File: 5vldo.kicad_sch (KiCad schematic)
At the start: 11 parts, among them IC1 TPS7A4501KTTR, IC2 TPS7A4501KTTR

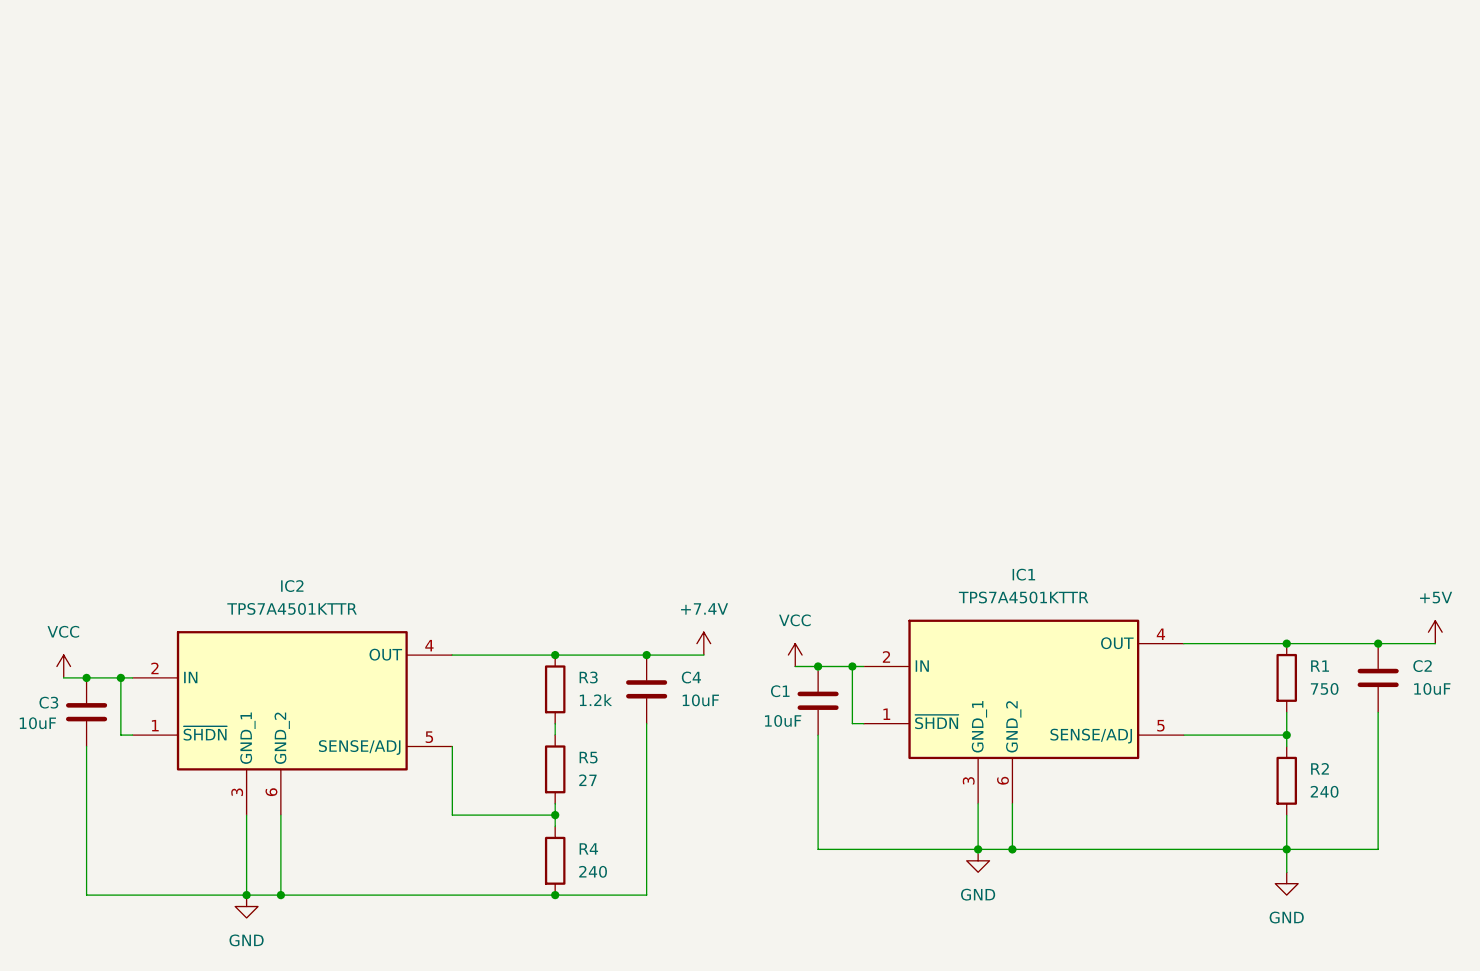
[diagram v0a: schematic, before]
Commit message: Fixed GPS, Radio, Baro, STM32, and added/rearanged some sheets (#26)
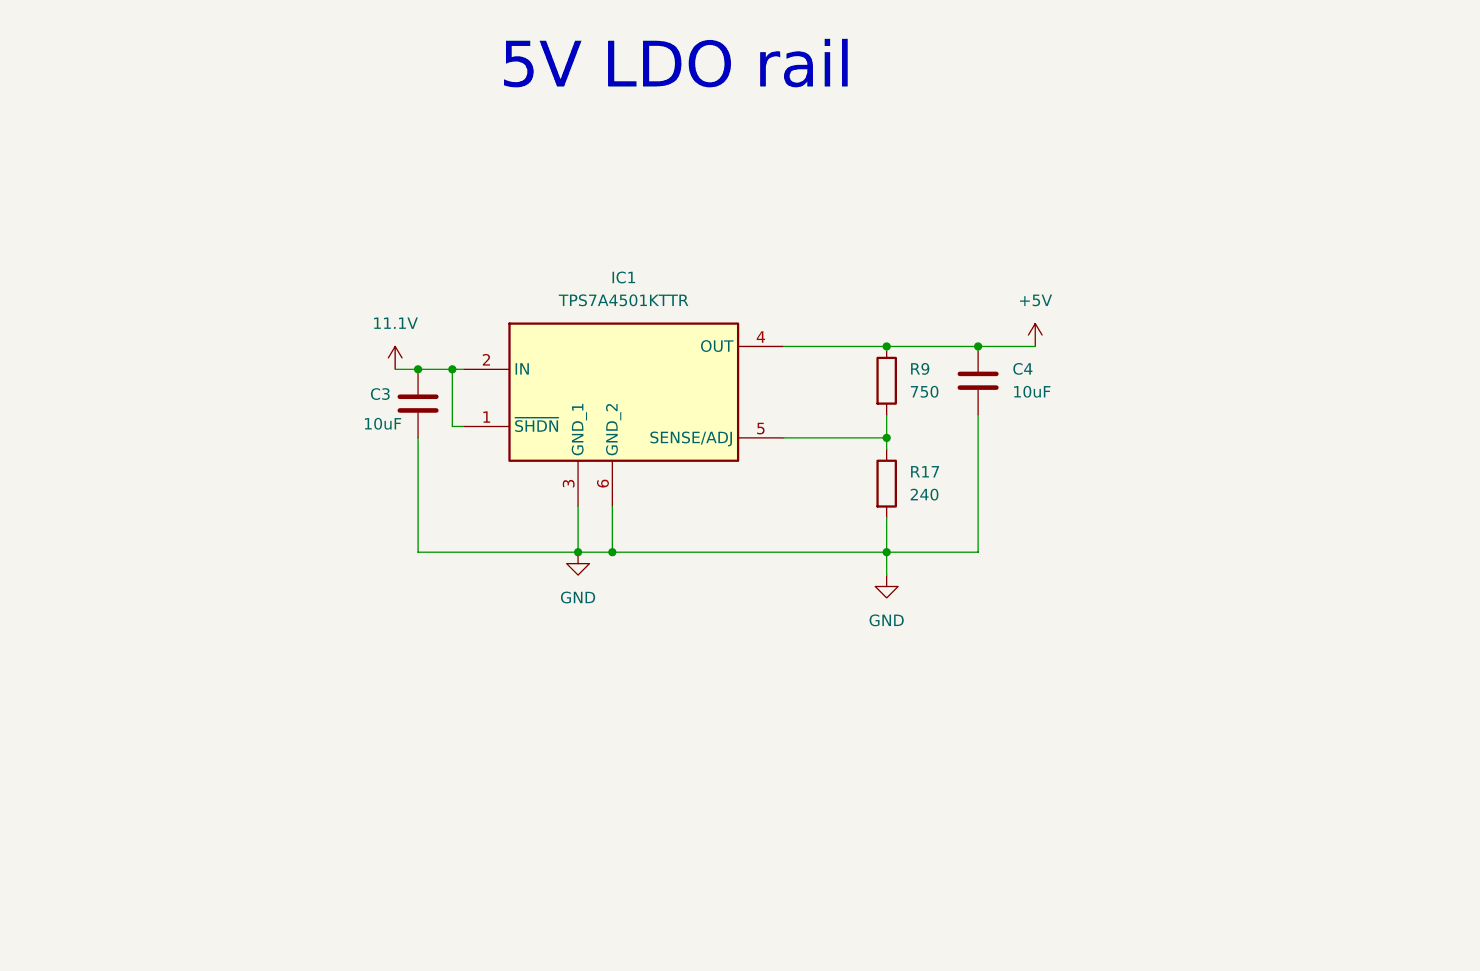
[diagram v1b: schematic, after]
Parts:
- removed C1, C2: 10uF, symbol Device:C
- removed IC2: TPS7A4501KTTR, TPS7A4501KTTR, symbol SamacSys_Parts:TPS7A4501KTTR
- removed R1: 750, symbol Device:R
- removed R2, R4: 240, symbol Device:R
- removed R3: 1.2k, symbol Device:R
- removed R5: 27, symbol Device:R
- added R17: 240, symbol Device:R
- added R9: 750, symbol Device:R
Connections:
- net +7.4V is gone; now on net +5V: C4.1
- net +5V: now also R9.1
- net GND: now also R17.2
- net at IC1.5 (SENSE/ADJ): now also R17.1, R9.2
- net VCC renamed 11.1V
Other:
- note added: "5V LDO rail"
